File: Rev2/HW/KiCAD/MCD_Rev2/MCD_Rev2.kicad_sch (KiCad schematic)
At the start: 77 parts, among them J1 DBUS_LOW, J2 DBUS_HIGH, J3 ABUS, J4 POWER, J5 JTAG, J6 Conn_01x02_Male, J7 DUART A, J8 DUART B, SW1 SW_Push, U1 XC9572XL-PC44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

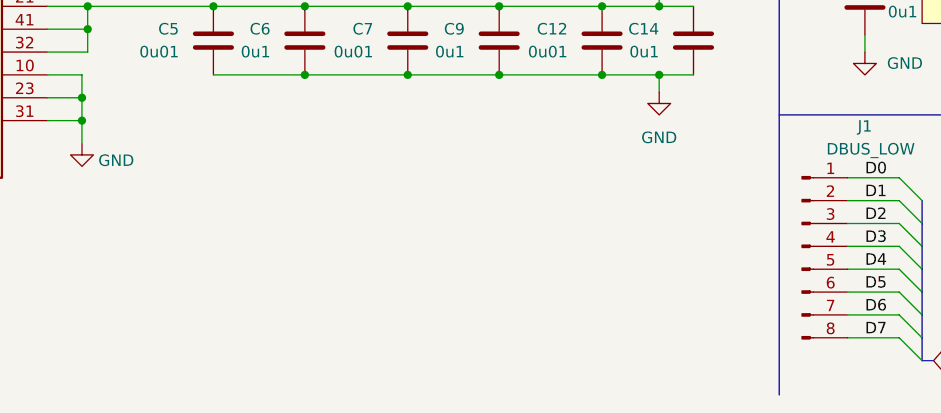
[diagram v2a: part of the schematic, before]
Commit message: added support for better commands and finished pcb rev3
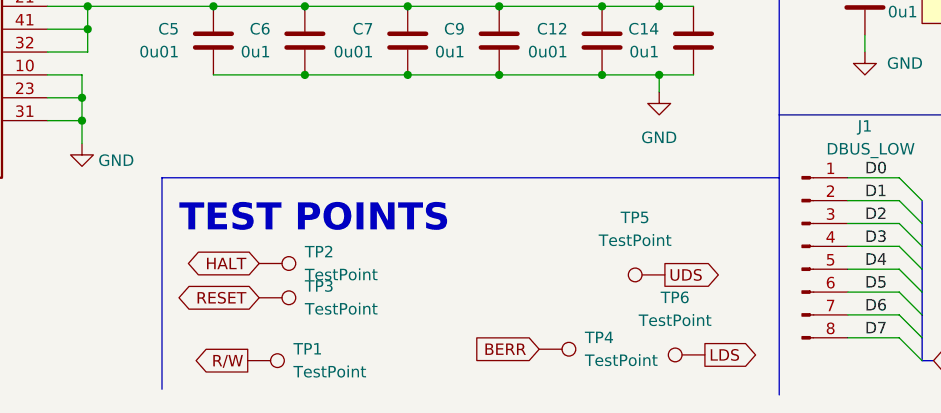
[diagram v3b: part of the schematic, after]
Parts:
- added TP1, TP2, TP3, TP4, TP5, TP6: TestPoint, TestPoint:TestPoint_Pad_D1.0mm, symbol Connector:TestPoint
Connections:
- net BERR: now also TP4.1
- net HALT: now also TP2.1
- net LDS: now also TP6.1
- net RESET: now also TP3.1
- net R/W: now also TP1.1
- net UDS: now also TP5.1
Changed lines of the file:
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@@
     (stroke (width 0) (type default) (color 0 0 0 0))
   )
+  (polyline (pts (xy 92.075 243.84) (xy 92.075 267.335))
+    (stroke (width 0) (type default) (color 0 0 0 0))
+  )
   (bus (pts (xy 106.045 115.57) (xy 106.045 118.11))
     (stroke (width 0) (type default) (color 0 0 0 0))
@@
     (stroke (width 0) (type default) (color 0 0 0 0))
   )
+  (polyline (pts (xy 160.655 243.84) (xy 92.075 243.84))
+    (stroke (width 0) (type default) (color 0 0 0 0))
+  )
   (wire (pts (xy 389.89 196.85) (xy 395.605 196.85))
     (stroke (width 0) (type default) (color 0 0 0 0))
@@
     (effects (font (size 1.27 1.27) (thickness 0.4) bold) (justify left bottom))
   )
+  (text "TEST POINTS\n" (at 93.98 250.19 0)
+    (effects (font (size 3 3) (thickness 0.6) bold) (justify left bottom))
+  )
   (text "PULL UP DUART DTACK?" (at 176.53 189.865 0)
     (effects (font (size 1.27 1.27)) (justify left bottom))
@@
     )
   )
+  (global_label "HALT" (shape bidirectional) (at 102.87 253.365 180) (fields_autoplaced)
+    (effects (font (size 1.27 1.27)) (justify right))
+    (property "Intersheet References" "${INTERSHEET_REFS}" (id 0) (at 96.0421 253.2856 0)
+      (effects (font (size 1.27 1.27)) (justify right) hide)
+    )
+  )
   (global_label "A21" (shape input) (at 27.94 208.28 180) (fields_autoplaced)
     (effects (font (size 1.27 1.27)) (justify right))
@@
     )
   )
+  (global_label "BERR" (shape input) (at 133.985 262.89 180) (fields_autoplaced)
+    (effects (font (size 1.27 1.27)) (justify right))
+    (property "Intersheet References" "${INTERSHEET_REFS}" (id 0) (at 126.6129 262.8106 0)
+      (effects (font (size 1.27 1.27)) (justify right) hide)
+    )
+  )
   (global_label "D[8..15]" (shape tri_state) (at 164.465 135.255 180) (fields_autoplaced)
     (effects (font (size 1.27 1.27)) (justify right))
@@
     )
   )
+  (global_label "RESET" (shape bidirectional) (at 102.87 257.175 180) (fields_autoplaced)
+    (effects (font (size 1.27 1.27)) (justify right))
+    (property "Intersheet References" "${INTERSHEET_REFS}" (id 0) (at 94.7117 257.0956 0)
+      (effects (font (size 1.27 1.27)) (justify right) hide)
+    )
+  )
   (global_label "TXDA" (shape input) (at 219.075 200.66 180) (fields_autoplaced)
     (effects (font (size 1.27 1.27)) (justify right))
@@
     )
   )
+  (global_label "LDS" (shape output) (at 152.4 263.525 0) (fields_autoplaced)
+    (effects (font (size 1.27 1.27)) (justify left))
+    (property "Intersheet References" "${INTERSHEET_REFS}" (id 0) (at 158.3207 263.4456 0)
+      (effects (font (size 1.27 1.27)) (justify left) hide)
+    )
+  )
   (global_label "DUART_DTACK" (shape output) (at 219.075 185.42 180) (fields_autoplaced)
     (effects (font (size 1.27 1.27)) (justify right))
@@
     )
   )
+  (global_label "R{slash}W" (shape output) (at 101.6 264.16 180) (fields_autoplaced)
+    (effects (font (size 1.27 1.27)) (justify right))
+    (property "Intersheet References" "${INTERSHEET_REFS}" (id 0) (at 95.135 264.0806 0)
+      (effects (font (size 1.27 1.27)) (justify right) hide)
+    )
+  )
   (global_label "TMS" (shape input) (at 256.54 147.955 180) (fields_autoplaced)
     (effects (font (size 1.27 1.27)) (justify right))
@@
     )
   )
+  (global_label "UDS" (shape output) (at 147.955 254.635 0) (fields_autoplaced)
+    (effects (font (size 1.27 1.27)) (justify left))
+    (property "Intersheet References" "${INTERSHEET_REFS}" (id 0) (at 154.1781 254.5556 0)
+      (effects (font (size 1.27 1.27)) (justify left) hide)
+    )
+  )
   (global_label "LED1" (shape input) (at 289.56 189.865 90) (fields_autoplaced)
     (effects (font (size 1.27 1.27)) (justify left))
@@
     (pin "1")
   )
+  (symbol (lib_id "Connector:TestPoint") (at 101.6 264.16 270) (unit 1)
+    (in_bom yes) (on_board yes) (fields_autoplaced)
+    (property "Reference" "TP1" (id 0) (at 106.68 262.8899 90)
+      (effects (font (size 1.27 1.27)) (justify left))
+    )
+    (property "Value" "TestPoint" (id 1) (at 106.68 265.4299 90)
+      (effects (font (size 1.27 1.27)) (justify left))
+    )
+    (property "Footprint" "TestPoint:TestPoint_Pad_D1.0mm" (id 2) (at 101.6 269.24 0)
+      (effects (font (size 1.27 1.27)) hide)
+    )
+    (property "Datasheet" "~" (id 3) (at 101.6 269.24 0)
+      (effects (font (size 1.27 1.27)) hide)
+    )
+    (pin "1")
+  )
   (symbol (lib_id "Device:R") (at 287.02 172.085 0) (unit 1)
     (in_bom yes) (on_board yes)
@@
     (pin "2")
   )
+  (symbol (lib_id "Connector:TestPoint") (at 152.4 263.525 90) (unit 1)
+    (in_bom yes) (on_board yes) (fields_autoplaced)
+    (property "Reference" "TP6" (id 0) (at 149.098 257.175 90))
+    (property "Value" "TestPoint" (id 1) (at 149.098 259.715 90))
+    (property "Footprint" "TestPoint:TestPoint_Pad_D1.0mm" (id 2) (at 152.4 258.445 0)
+      (effects (font (size 1.27 1.27)) hide)
+    )
+    (property "Datasheet" "~" (id 3) (at 152.4 258.445 0)
+      (effects (font (size 1.27 1.27)) hide)
+    )
+    (pin "1")
+  )
   (symbol (lib_id "Imported:AP2114HA-3.3TRG1") (at 260.985 40.005 0) (unit 1)
     (in_bom yes) (on_board yes) (fields_autoplaced)
@@
     (pin "2")
   )
+  (symbol (lib_id "Connector:TestPoint") (at 102.87 257.175 270) (unit 1)
+    (in_bom yes) (on_board yes) (fields_autoplaced)
+    (property "Reference" "TP3" (id 0) (at 107.95 255.9049 90)
+      (effects (font (size 1.27 1.27)) (justify left))
+    )
+    (property "Value" "TestPoint" (id 1) (at 107.95 258.4449 90)
+      (effects (font (size 1.27 1.27)) (justify left))
+    )
+    (property "Footprint" "TestPoint:TestPoint_Pad_D1.0mm" (id 2) (at 102.87 262.255 0)
+      (effects (font (size 1.27 1.27)) hide)
+    )
+    (property "Datasheet" "~" (id 3) (at 102.87 262.255 0)
+      (effects (font (size 1.27 1.27)) hide)
+    )
+    (pin "1")
+  )
   (symbol (lib_id "Device:R") (at 101.6 172.72 0) (unit 1)
     (in_bom yes) (on_board yes)
@@
     (pin "2")
   )
+  (symbol (lib_id "Connector:TestPoint") (at 102.87 253.365 270) (unit 1)
+    (in_bom yes) (on_board yes) (fields_autoplaced)
+    (property "Reference" "TP2" (id 0) (at 107.95 252.0949 90)
+      (effects (font (size 1.27 1.27)) (justify left))
+    )
+    (property "Value" "TestPoint" (id 1) (at 107.95 254.6349 90)
+      (effects (font (size 1.27 1.27)) (justify left))
+    )
+    (property "Footprint" "TestPoint:TestPoint_Pad_D1.0mm" (id 2) (at 102.87 258.445 0)
+      (effects (font (size 1.27 1.27)) hide)
+    )
+    (property "Datasheet" "~" (id 3) (at 102.87 258.445 0)
+      (effects (font (size 1.27 1.27)) hide)
+    )
+    (pin "1")
+  )
   (symbol (lib_id "Device:C") (at 97.79 228.6 0) (mirror y) (unit 1)
     (in_bom yes) (on_board yes) (fields_autoplaced)
@@
     (pin "3")
   )
+  (symbol (lib_id "Connector:TestPoint") (at 147.955 254.635 90) (unit 1)
+    (in_bom yes) (on_board yes) (fields_autoplaced)
+    (property "Reference" "TP5" (id 0) (at 144.653 248.285 90))
+    (property "Value" "TestPoint" (id 1) (at 144.653 250.825 90))
+    (property "Footprint" "TestPoint:TestPoint_Pad_D1.0mm" (id 2) (at 147.955 249.555 0)
+      (effects (font (size 1.27 1.27)) hide)
+    )
+    (property "Datasheet" "~" (id 3) (at 147.955 249.555 0)
+      (effects (font (size 1.27 1.27)) hide)
+    )
+    (pin "1")
+  )
   (symbol (lib_id "power:GND") (at 137.16 39.37 0) (unit 1)
     (in_bom yes) (on_board yes) (fields_autoplaced)
@@
     (pin "2")
   )
+  (symbol (lib_id "Connector:TestPoint") (at 133.985 262.89 270) (unit 1)
+    (in_bom yes) (on_board yes) (fields_autoplaced)
+    (property "Reference" "TP4" (id 0) (at 139.065 261.6199 90)
+      (effects (font (size 1.27 1.27)) (justify left))
+    )
+    (property "Value" "TestPoint" (id 1) (at 139.065 264.1599 90)
+      (effects (font (size 1.27 1.27)) (justify left))
+    )
+    (property "Footprint" "TestPoint:TestPoint_Pad_D1.0mm" (id 2) (at 133.985 267.97 0)
+      (effects (font (size 1.27 1.27)) hide)
+    )
+    (property "Datasheet" "~" (id 3) (at 133.985 267.97 0)
+      (effects (font (size 1.27 1.27)) hide)
+    )
+    (pin "1")
+  )
   (symbol (lib_id "Device:C") (at 379.095 33.655 0) (unit 1)
     (in_bom yes) (on_board yes) (fields_autoplaced)
@@
       (reference "SW1") (unit 1) (value "SW_Push") (footprint "Button_Switch_THT:SW_PUSH_6mm")
     )
+    (path "/255c4a6d-3a18-43e6-891a-672d4a760771"
+      (reference "TP1") (unit 1) (value "TestPoint") (footprint "TestPoint:TestPoint_Pad_D1.0mm")
+    )
+    (path "/84addbe9-4a56-4475-ab2c-50c5cc5f74b1"
+      (reference "TP2") (unit 1) (value "TestPoint") (footprint "TestPoint:TestPoint_Pad_D1.0mm")
+    )
+    (path "/7c3d33e0-4f54-4e50-a4b0-7bbcb9d54e8b"
+      (reference "TP3") (unit 1) (value "TestPoint") (footprint "TestPoint:TestPoint_Pad_D1.0mm")
+    )
+    (path "/d4dc564e-2442-40d6-8278-d908e551ee12"
+      (reference "TP4") (unit 1) (value "TestPoint") (footprint "TestPoint:TestPoint_Pad_D1.0mm")
+    )
+    (path "/baa0fb14-9a9f-497a-ae19-da95224f4aed"
+      (reference "TP5") (unit 1) (value "TestPoint") (footprint "TestPoint:TestPoint_Pad_D1.0mm")
+    )
+    (path "/4d72b1ac-c0f7-4cb8-8233-3efaeb0fa4a5"
+      (reference "TP6") (unit 1) (value "TestPoint") (footprint "TestPoint:TestPoint_Pad_D1.0mm")
+    )
     (path "/498c61a7-be36-43cd-90df-6e60f0c85fa5"
